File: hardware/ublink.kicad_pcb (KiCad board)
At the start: 2 copper layers, 67 x 54.5 mm, 62 parts, among them J1 USB_B_Micro, J2 AC1, J3 5V Trafo, J4 Screw_Terminal_01x02, J5 Screw_Terminal_01x02, J7 Screw_Terminal_01x02, J8 JTAG/UART, J9 Screw_Terminal_01x02, Q1 STN3NF06L, Q2 RU6099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

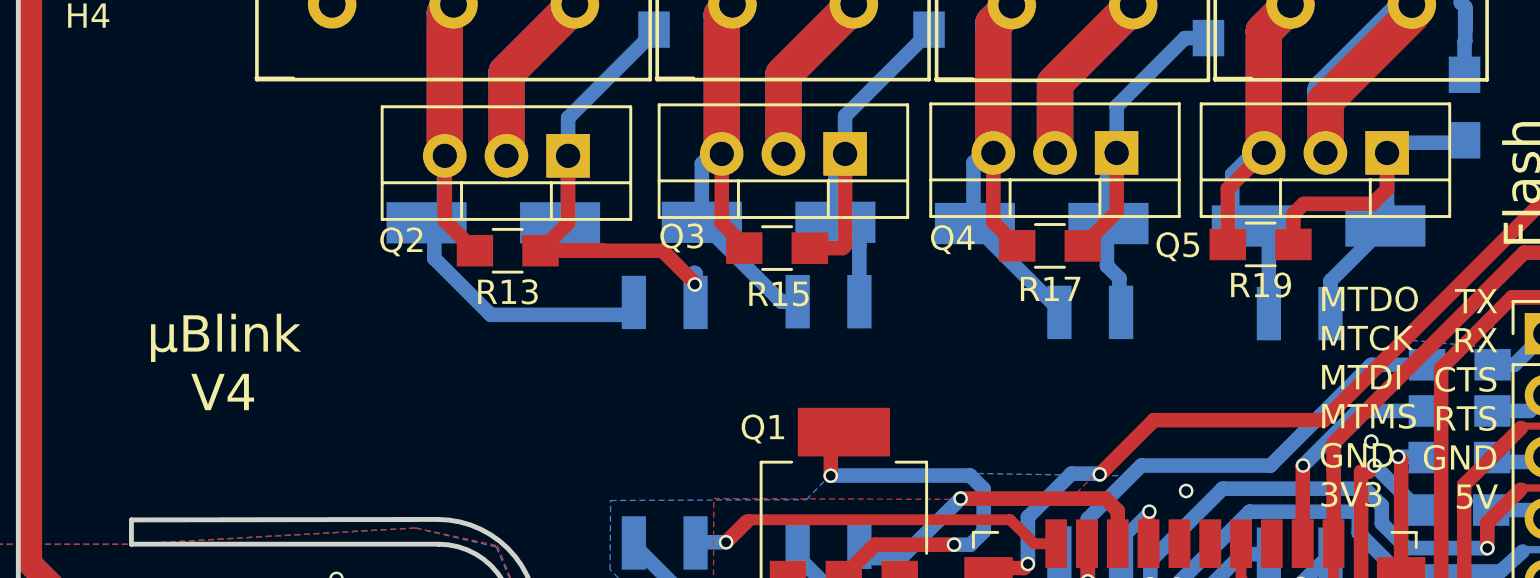
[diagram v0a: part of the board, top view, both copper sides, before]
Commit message: Delete superflous resistors
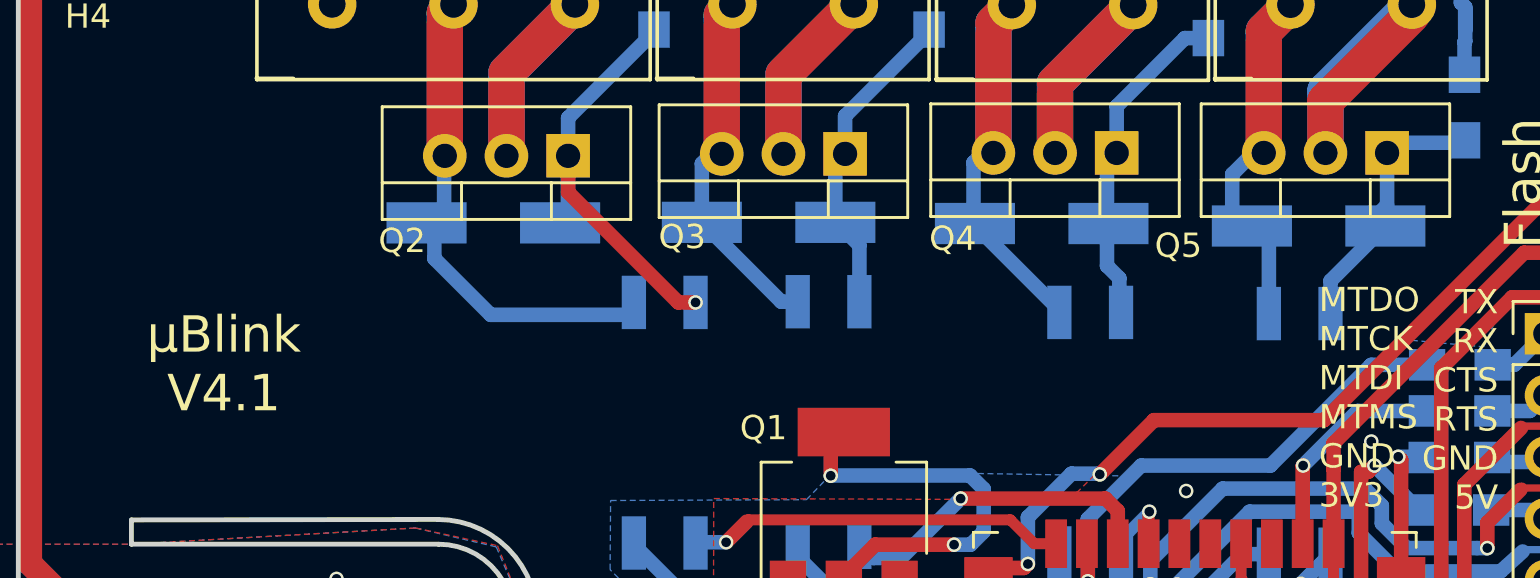
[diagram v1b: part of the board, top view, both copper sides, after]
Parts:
- removed the R13 at (130.3, 104.9)
- removed the R15 at (141.4, 104.8)
- removed R17, R19: 33k, Resistors_SMD:R_0805_HandSoldering
- renumbered R14 to R13, R16 to R14, R18 to R15
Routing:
- net /W_GATE: track 19.1 -> 12.1 mm
- net /R_GATE: track 25.3 -> 18.8 mm
- net /G_GATE: track 18.5 -> 13.2 mm
- net /R_GND: track 30.4 -> 26.0 mm
- net /B_GATE: track 20.2 -> 15.8 mm
- net /W_GND: track 26.9 -> 22.5 mm
- net /G_GND: track 25.5 -> 21.2 mm
- net /B_GND: track 26.1 -> 21.9 mm
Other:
- board text added: "µBlink V4.1"
- board text removed: "µBlink V4"

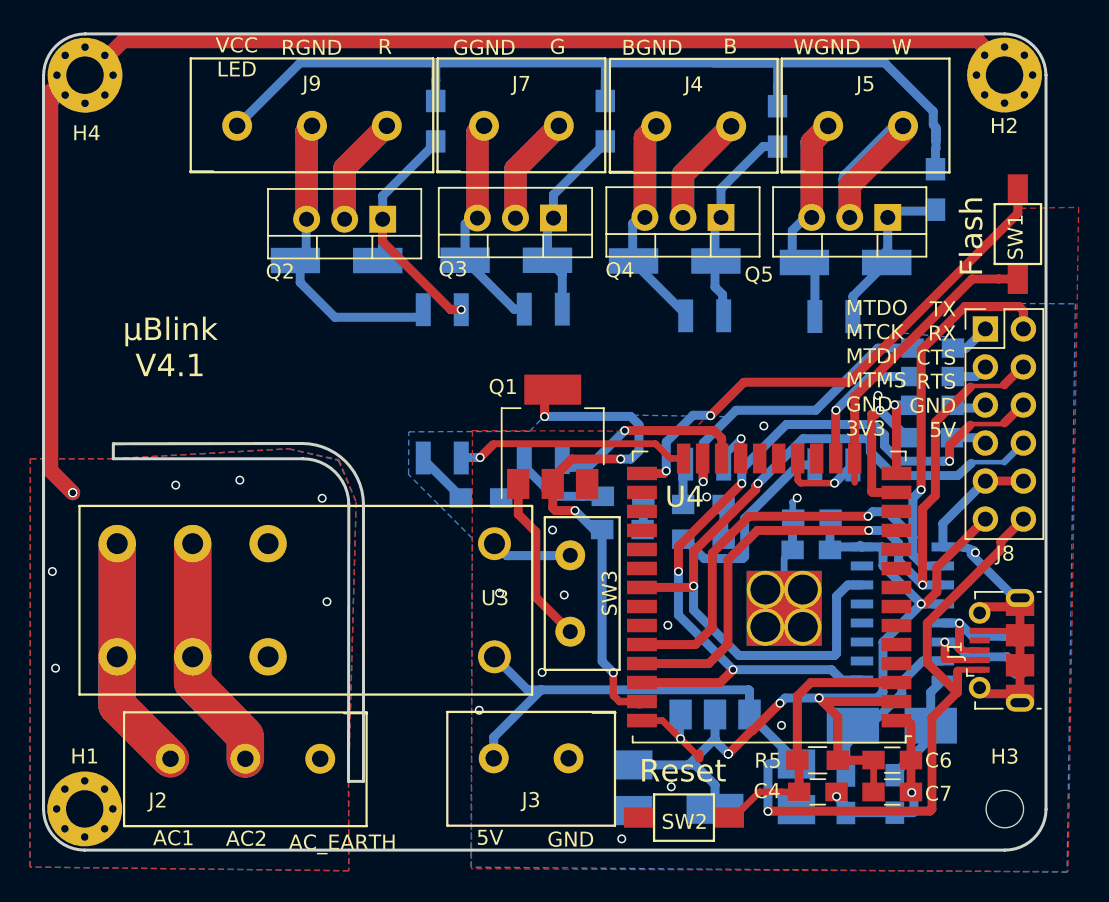
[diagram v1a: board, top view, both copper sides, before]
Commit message: Fix layout errors
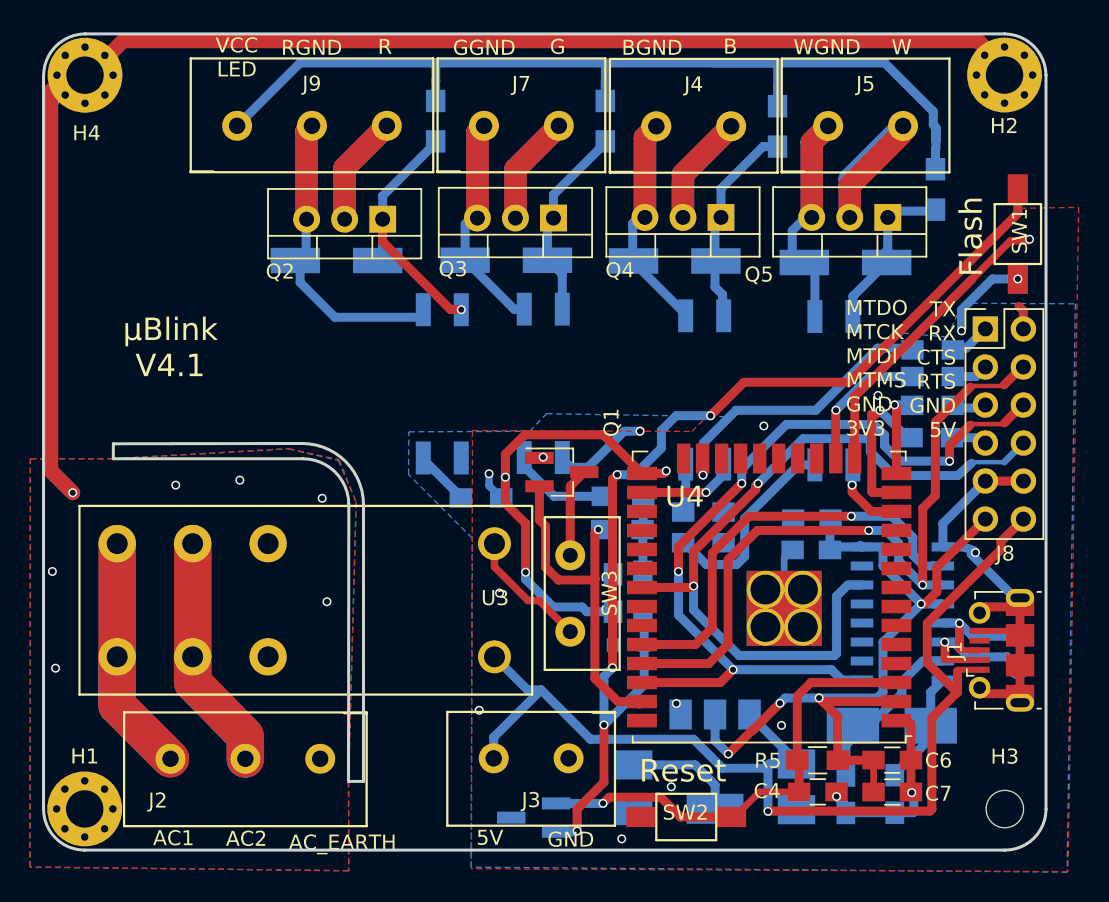
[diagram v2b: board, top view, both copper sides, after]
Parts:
- added C2: 2u, Capacitors_SMD:C_0805_HandSoldering, B.Cu at (148.2, 126.0)
- added D5: D, Diodes_SMD:D_0805, B.Cu at (149.2, 129.4)
- added Q6: NMOS, TO_SOT_Packages_SMD:SOT-23_Handsoldering, B.Cu at (142.9, 141.0)
- added R6: 10k, Resistors_SMD:R_0805_HandSoldering, B.Cu at (150.2, 125.9)
- Q1: footprint ublink:STN3NF06L -> TO_SOT_Packages_SMD:SOT-23_Handsoldering
- moved Q1 2.44 mm to (144.8, 117.9), turned to 0 degrees
- moved R10 0.51 mm to (154.2, 120.6)
- moved R11 0.24 mm to (154.2, 122.6)
- moved SW2 0.16 mm to (153.1, 140.9), turned to 180 degrees
- moved R4 0.12 mm to (169.5, 109.7)
- turned SW1 to 270 degrees
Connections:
- C4 pad 1: Net-(C4-Pad1) -> EN
- J8 pad 2: TX -> Net-(J8-Pad2)
- Q1 pad 1: Net-(Q1-Pad1) -> GND
- Q1 pad 3: GND -> Net-(Q1-Pad3)
- R5 pad 2: Net-(C4-Pad1) -> EN
- SW1 pad 1: GND -> Net-(D5-Pad2)
- SW1 pad 2: Net-(SW1-Pad2) -> 3V3
- SW2 pad 1: GND -> EN
- SW2 pad 2: Net-(C4-Pad1) -> GND
- SW3 pad 1: Net-(Q1-Pad1) -> Net-(SW3-Pad1)
- SW3 pad 2: Net-(SW3-Pad2) -> Net-(Q1-Pad3)
- U3 pad 2: Net-(SW3-Pad2) -> Net-(SW3-Pad1)
- U4 pad 12: Net-(U4-Pad12) -> W_CTRL
- U4 pad 18: W_CTRL -> Net-(U4-Pad18)
- U4 pad 21: B_CTRL -> Net-(U4-Pad21)
- U4 pad 22: G_CTRL -> Net-(U4-Pad22)
- U4 pad 24: R_CTRL -> Net-(U4-Pad24)
- U4 pad 25: Net-(SW1-Pad2) -> FLASH
- U4 pad 26: Net-(U4-Pad26) -> B_CTRL
- U4 pad 27: Net-(U4-Pad27) -> G_CTRL
- U4 pad 28: Net-(U4-Pad28) -> R_CTRL
- U4 pad 3: Net-(C4-Pad1) -> EN
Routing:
- net Net-(D5-Pad2): track 0.00 -> 71.4 mm, vias 0 -> 5
- net Net-(SW1-Pad2): track 35.1 -> 0.00 mm, vias 2 -> 0
- net EN: track 0.00 -> 31.2 mm, vias 0 -> 1
- net FLASH: track 0.00 -> 30.3 mm, vias 0 -> 3
- net TX: track 51.0 -> 28.6 mm, vias 2 -> 1
- net Net-(C4-Pad1): track 18.8 -> 0.00 mm
- net R_CTRL: track 15.6 -> 0.03 mm, vias 1 -> 0
- net RELAIS_CTRL: track 36.5 -> 23.3 mm, vias 4 -> 1
- net Net-(Q1-Pad1): track 11.3 -> 0.00 mm
- net Net-(SW3-Pad1): track 0.00 -> 8.41 mm
- net GND: track 79.2 -> 71.8 mm, vias 17 -> 14
- net G_CTRL: track 13.4 -> 6.45 mm
- net Net-(Q1-Pad3): track 0.00 -> 5.95 mm
- net Net-(SW3-Pad2): track 4.94 -> 0.00 mm
- net 3V3: track 67.1 -> 70.5 mm, vias 5 -> 6
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
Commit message: Initial firmware
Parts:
- moved R11 0.22 mm to (154.1, 122.8)
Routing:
- net 3V3: track 70.5 -> 91.5 mm, vias 6 -> 8
- net /LED_VCC: track 66.6 -> 61.5 mm
- net AC2: track 31.7 -> 35.5 mm
- net CTS: track 55.7 -> 57.8 mm
- net RTS: track 51.3 -> 53.0 mm
- net /B_GATE: track 15.8 -> 17.5 mm
- net Net-(C3-Pad1): track 7.88 -> 9.54 mm
- net /R_GATE: track 18.8 -> 20.3 mm
- net AC_SAFE: track 121.9 -> 123.4 mm
- net AC1: track 31.3 -> 32.8 mm
- net /USB_D-: track 8.23 -> 9.65 mm
- net B_CTRL: track 6.66 -> 7.89 mm
- net EN: track 31.2 -> 32.4 mm
- net Net-(R11-Pad2): track 13.8 -> 14.9 mm
- net RX: track 47.9 -> 48.9 mm
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
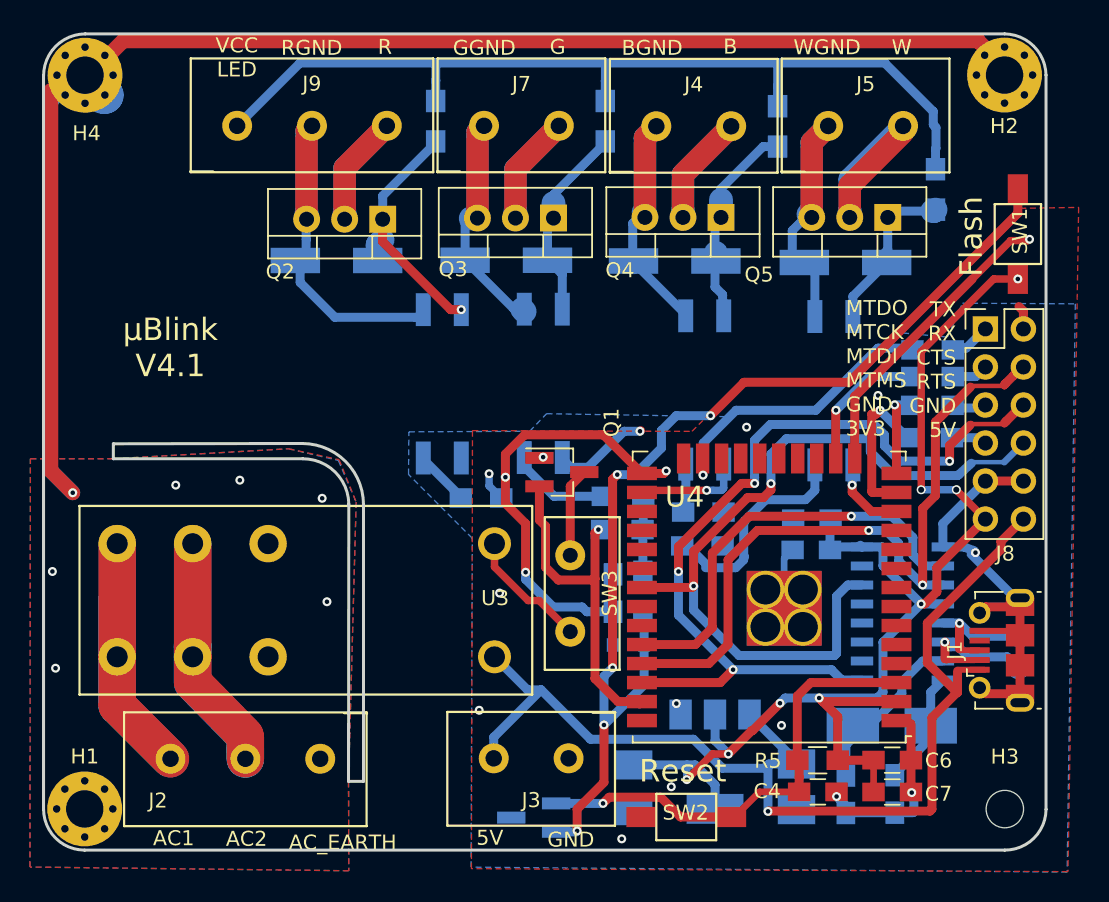
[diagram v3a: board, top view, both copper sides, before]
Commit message: v5 PCB: Flash button nau auto resets
Flash button exposed via pin headers; no more UART
via pin headers.

Lights are on pins that can actually be used.
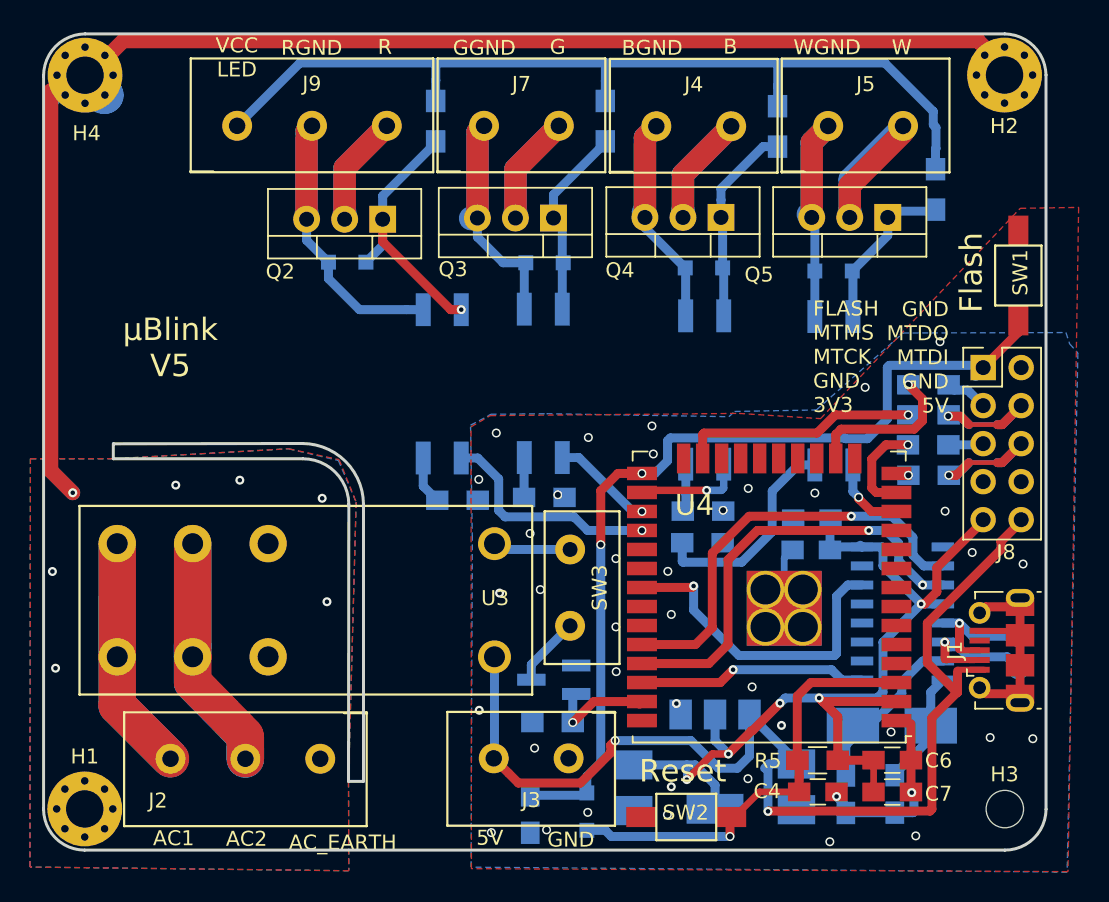
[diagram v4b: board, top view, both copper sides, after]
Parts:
- removed C2: 2u, Capacitors_SMD:C_0805_HandSoldering
- removed Q6: NMOS, TO_SOT_Packages_SMD:SOT-23_Handsoldering
- removed R6: 10k, Resistors_SMD:R_0805_HandSoldering
- added 2u2: CP2, Capacitors_SMD:C_0805_HandSoldering, B.Cu at (142.6, 140.7)
- D1, D2, D3, D4: footprint Diodes_SMD:D_MiniMELF_Handsoldering -> Diodes_SMD:D_SOD-323_HandSoldering
- D5: footprint Diodes_SMD:D_0805 -> Diodes_SMD:D_SOD-323_HandSoldering
- J8: footprint Pin_Headers:Pin_Header_Straight_2x06_Pitch2.54mm -> Pin_Headers:Pin_Header_Straight_2x05_Pitch2.54mm
- Q1: moved to B.Cu
- moved Q1 13.9 mm to (144.2, 131.8), turned to 180 degrees
- moved R7 13.7 mm to (144.1, 134.6), turned to 180 degrees
- moved D5 11.5 mm to (146.4, 140.6), turned to 270 degrees
- moved R9 5.26 mm to (143.6, 119.6)
- moved R2 4.68 mm to (169.2, 118.1), turned to 180 degrees
- moved R4 4.35 mm to (169.2, 114.1), turned to 180 degrees
- moved SW1 2.77 mm to (175.2, 104.8)
- moved J8 2.58 mm to (172.9, 110.9)
- moved D2 2.56 mm to (143.6, 103.9)
- moved D3 2.00 mm to (154.2, 104.2)
- moved R8 1.58 mm to (137.8, 119.8)
- moved D4 0.98 mm to (162.9, 104.5)
- moved D1 0.72 mm to (130.4, 103.9)
- moved R3 0.61 mm to (169.2, 112.1)
- moved R1 0.53 mm to (169.2, 116.1)
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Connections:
- net /MTCK renamed MTCK
- net /MTMS renamed MTMS
- D5 pad 2: Net-(D5-Pad2) -> EN
- J8 pad 1: Net-(J8-Pad1) -> FLASH
- J8 pad 10: GND -> 5V
- J8 pad 2: Net-(J8-Pad2) -> GND
- J8 pad 4: RX -> Net-(J8-Pad4)
- J8 pad 6: CTS -> Net-(J8-Pad6)
- J8 pad 7: Net-(J8-Pad7) -> GND
- J8 pad 8: RTS -> GND
- J8 pad 9: GND -> 3V3
- R1 pad 2: Net-(J8-Pad7) -> Net-(J8-Pad5)
- R2 pad 1: /MTDI -> Net-(J8-Pad6)
- R2 pad 2: Net-(J8-Pad5) -> MTDI
- R4 pad 1: /MTDO -> Net-(J8-Pad4)
- R4 pad 2: Net-(J8-Pad1) -> MTDO
- SW1 pad 1: Net-(D5-Pad2) -> GND
- SW1 pad 2: 3V3 -> FLASH
- SW3 pad 1: Net-(SW3-Pad1) -> Net-(Q1-Pad3)
- SW3 pad 2: Net-(Q1-Pad3) -> Net-(SW3-Pad2)
- U3 pad 2: Net-(SW3-Pad1) -> Net-(SW3-Pad2)
- U4 pad 14: /MTDI -> MTDI
- U4 pad 23: /MTDO -> MTDO
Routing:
- net Net-(D5-Pad2): track 71.4 -> 0.00 mm, vias 5 -> 0
- net CTS: track 57.8 -> 15.3 mm, vias 4 -> 1
- net GND: track 71.8 -> 30.2 mm, vias 14 -> 40
- net RTS: track 53.0 -> 21.8 mm, vias 2 -> 1
- net FLASH: track 30.3 -> 61.4 mm, vias 3 -> 2
- net 3V3: track 91.5 -> 68.5 mm, vias 8 -> 5
- net /MTDO: track 20.0 -> 0.00 mm, vias 1 -> 0
- net RX: track 48.9 -> 29.3 mm
- net RELAIS_CTRL: track 23.6 -> 7.45 mm
- net MTDO: track 0.00 -> 15.9 mm, vias 0 -> 1
- net R_CTRL: track 0.04 -> 15.3 mm, vias 0 -> 1
- net Net-(J8-Pad6): track 0.00 -> 10.7 mm, vias 0 -> 1
- net Net-(J8-Pad4): track 0.00 -> 10.5 mm, vias 0 -> 1
- net Net-(SW3-Pad1): track 8.41 -> 0.00 mm
- net /MTDI: track 6.07 -> 0.00 mm, vias 1 -> 0
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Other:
- board text added: "FLASH MTMS MTCK GND 3V3"
- board text added: "GND MTDO MTDI GND 5V"
- board text added: "µBlink V5"
- board text removed: "MTDO MTCK MTDI MTMS GND 3V3"
- board text removed: "TX RX CTS RTS GND 5V"
- board text removed: "µBlink V4.1"

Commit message: Hardware v5.1: Reset when DTR is high
This allows esptool.py to reset the µC and boot into
uart downloader mode without the user having to press
a button.
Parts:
- added Q6: STN3NF06L, TO_SOT_Packages_SMD:SOT-23_Handsoldering, B.Cu at (151.8, 127.1)
- J8: value JTAG/UART -> Pin Header
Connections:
- Q1 pad 1: GND -> Net-(Q1-Pad1)
- Q1 pad 3: Net-(Q1-Pad3) -> GND
- SW3 pad 1: Net-(Q1-Pad3) -> Net-(Q1-Pad1)
- U2 pad 13: Net-(U2-Pad13) -> DTR
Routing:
- net DTR: track 0.00 -> 25.8 mm, vias 0 -> 4
- net Net-(Q1-Pad3): track 4.67 -> 0.00 mm
- net FLASH: track 61.4 -> 64.3 mm
- net Net-(Q1-Pad1): track 0.00 -> 2.82 mm
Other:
- board text added: "µBlink V5.1"
- board text removed: "µBlink V5"

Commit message: stash
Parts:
- removed 2u2: CP2, Capacitors_SMD:C_0805_HandSoldering
- removed D5: D, Diodes_SMD:D_SOD-323_HandSoldering
- added C2: 2u, Capacitors_SMD:C_0805_HandSoldering, B.Cu at (148.1, 124.4)
- added Q7: STN3NF06L, TO_SOT_Packages_SMD:SOT-23_Handsoldering, B.Cu at (152.7, 129.8)
- added Q8: STN3NF06L, TO_SOT_Packages_SMD:SOT-23_Handsoldering, B.Cu at (152.7, 126.0)
- added R6: 10k, Resistors_SMD:R_0805_HandSoldering, B.Cu at (140.2, 140.5)
- moved Q6 15.1 mm to (144.2, 140.1), turned to 180 degrees
- moved R7 4.23 mm to (147.1, 131.6), turned to 90 degrees
- moved Q1 2.68 mm to (142.3, 133.6)
- moved 10u1 0.62 mm to (160.9, 120.7)
- moved C5 0.57 mm to (160.9, 122.8)
- moved R3 0.32 mm to (169.2, 111.7)
- moved R1 0.32 mm to (169.2, 115.7)
- moved R2 0.32 mm to (169.2, 117.8)
- moved R4 0.32 mm to (169.2, 113.7)
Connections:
- J8 pad 1: FLASH -> FLASH_BTN
- J8 pad 2: GND -> 3V3
- Q6 pad 1: FLASH -> EN
- Q6 pad 2: DTR -> FLASH_BTN
- Q6 pad 3: RTS -> GND
- SW1 pad 1: GND -> FLASH_BTN
- SW1 pad 2: FLASH -> 3V3
- SW2 pad 1: EN -> GND
- SW2 pad 2: GND -> EN
- U2 pad 9: CTS -> Net-(U2-Pad9)
- U4 pad 11: Net-(U4-Pad11) -> EN
- U4 pad 31: RTS -> Net-(U4-Pad31)
- U4 pad 36: CTS -> Net-(U4-Pad36)
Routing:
- net FLASH_BTN: track 0.00 -> 79.3 mm, vias 0 -> 1
- net FLASH: track 64.3 -> 40.2 mm, vias 2 -> 3
- net 3V3: track 68.5 -> 90.7 mm
- net EN: track 31.2 -> 52.1 mm, vias 1 -> 2
- net TX: track 29.6 -> 45.9 mm
- net RX: track 29.3 -> 45.3 mm, vias 2 -> 3
- net CTS: track 15.3 -> 0.00 mm, vias 1 -> 0
- net B_CTRL: track 7.89 -> 17.8 mm
- net RTS: track 21.8 -> 29.2 mm, vias 1 -> 0
- net DTR: track 25.8 -> 19.4 mm, vias 4 -> 2
- net Net-(J8-Pad6): track 10.7 -> 5.29 mm, vias 1 -> 0
- net Net-(J8-Pad4): track 10.5 -> 5.63 mm, vias 1 -> 0
- net GND: track 30.2 -> 26.1 mm
- net Net-(Q1-Pad1): track 2.82 -> 6.42 mm
- net 5V: track 78.0 -> 76.2 mm, vias 2 -> 3
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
